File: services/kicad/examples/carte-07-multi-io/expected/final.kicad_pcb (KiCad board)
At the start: 2 copper layers, 99.5 x 79.8 mm, 44 parts, among them J1 IN_5V, J10 IO0, J11 IO1, J12 IO2, J2 SWD, U1 STM32F103C8T6, U2 AMS1117-3.3

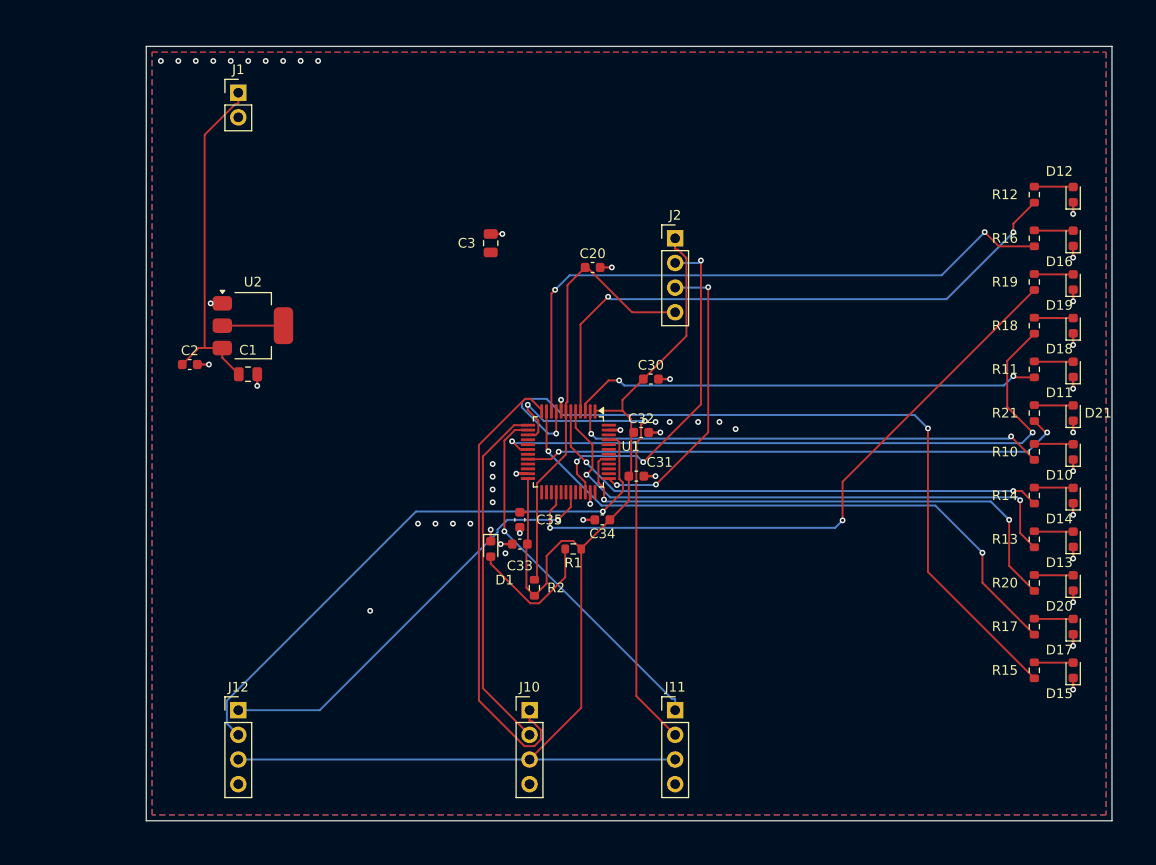
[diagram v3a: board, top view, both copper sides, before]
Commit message: chore(banc): relivrer carte-01..10 avec la couture corrigee
Boards reroutes par HTTP depuis placement.kicad_pcb inchange, avec le
code de #217. Juges par remesurer_banc.py : 0 erreur, 0 connexion
manquante sur les dix. 678 -> 443 vias ; la rangee de vias GND du bord
haut a disparu.

mesures.json : `board` recompte, `drc_du_board` rejuge, nouvelle cle
`couture_corrigee` (date, vias_avant, couches). journal.txt et les
champs du run d origine sont laisses tels quels et le disent.
rendu-3d.png : kicad-cli, modeles 3D, iso 1400x900.

Couches d un tirage : huit cartes sur 2, carte-08 et carte-10 sur 4.
CLAUDE.md et BANC_DRIVER_LLM.md recomptes. carte-11 non touchee.

Co-Authored-By: Claude Opus 5 (1M context) <noreply@anthropic.com>
Claude-Session: https://claude.ai/code/session_01TnMqm4La2CxQHHB5K8aSSV
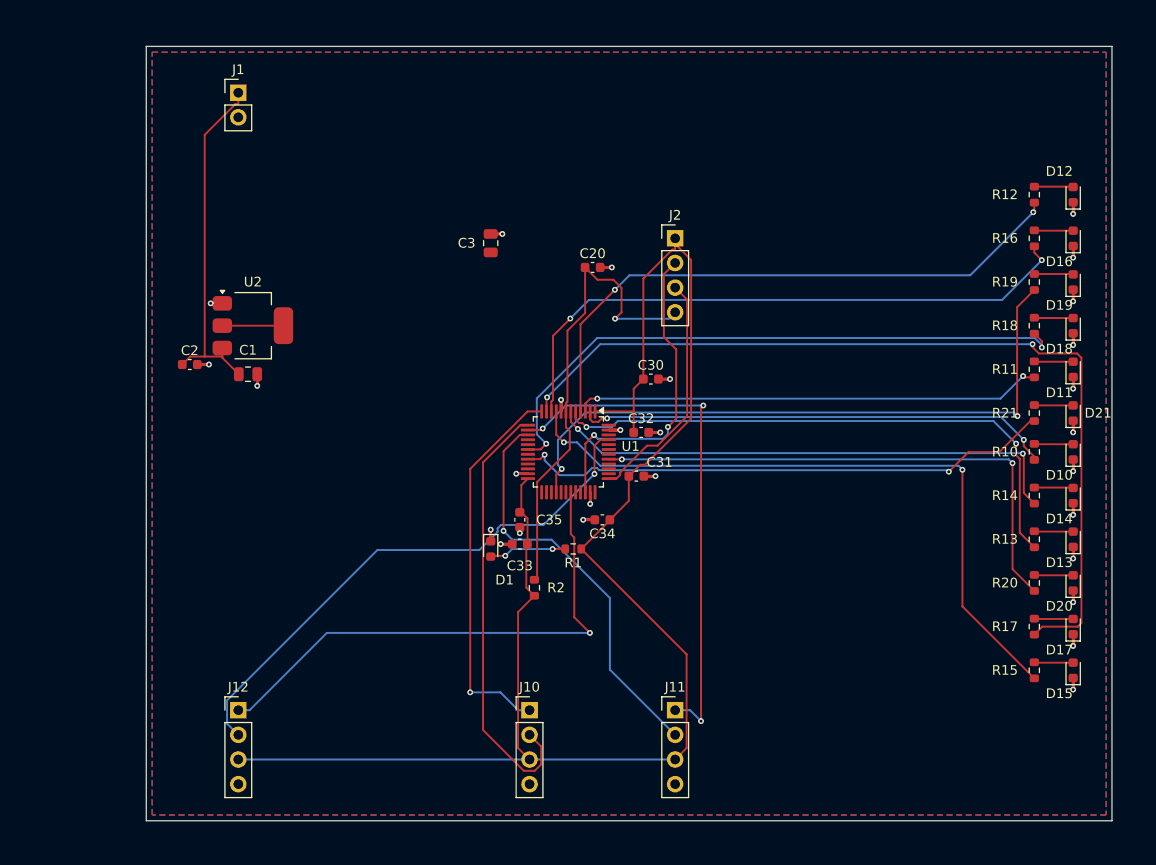
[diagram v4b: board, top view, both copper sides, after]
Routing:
- net GND: track 36.6 -> 103.8 mm, vias 53 -> 28
- net +3V3: track 132.4 -> 165.9 mm
- net IO_L7: track 63.9 -> 92.2 mm
- net EXT1_1: track 38.1 -> 54.8 mm, vias 1 -> 3
- net IO_L5: track 81.0 -> 70.3 mm
- net EXT2_1: track 44.6 -> 54.8 mm
- net EXT1_2: track 51.6 -> 42.1 mm, vias 2 -> 1
- net EXT0_2: track 36.6 -> 45.3 mm
- net EXT0_1: track 47.7 -> 39.7 mm, vias 0 -> 1
- net SWCLK: track 31.1 -> 24.6 mm, vias 3 -> 0
- net LED_PWR: track 14.1 -> 8.00 mm, vias 0 -> 2
- net IO_L8: track 68.6 -> 64.1 mm
- net EXT2_2: track 60.2 -> 56.4 mm
- net NRST: track 45.5 -> 49.2 mm, vias 0 -> 1
- net SWDIO: track 36.9 -> 33.2 mm, vias 3 -> 2
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
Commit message: fix(banc): le contour n etait JAMAIS resserre — dix cartes divisees par 2 a 4
Question de l utilisateur devant les rendus : « tu es satisfait de ce
placement ? ». Non, et la mesure lui donnait raison.

    carte-10 livree     140 x 105 mm = 14725 mm2
    son circuit          51 x  66 mm =  3366 mm2
    OCCUPATION                            23 %
    connecteurs                      56 a 75 mm du circuit
    fil de signal                      1230 mm  (VIN a lui seul 112 mm)

LA CAUSE : `run_pipeline.py` n envoyait pas `auto_size_board` a `/place/auto`.
Le resserrement du contour sur le placement existe depuis le 2026-09-13 et ne
s execute que si l appelant l autorise ; le defaut du modele est `False`.

C est le SEPTIEME levier de ce projet qui existe et que personne n appelle,
apres max_distance_mm, anchor_pin, WorkflowConfig.grid, constraints,
move_reference, bottom_up_placement et LocalRerouter.

⚠️ Et il etait INVISIBLE : la chaine de PRODUCTION passe bien le drapeau depuis
`handlePlacement`. Le banc mesurait donc un comportement que le produit n a
pas — l inverse exact de ce a quoi sert un banc.

MESURE APRES CORRECTION, meme circuit, meme graine :

    carte             demandee      REELLE        err  manq
    carte-01           25 x 20     20,1 x 14,6     0    0
    carte-02           55 x 40     34,9 x 25,4     0    0
    carte-03           50 x 35     26,1 x 20,1     0    0
    carte-04           60 x 45     36,6 x 27,2     0    0
    carte-05           70 x 50     43,6 x 32,6     0    0
    carte-06           80 x 60     48,5 x 36,4     0    0
    carte-07          110 x 80     53,2 x 38,8     0    0
    carte-08          125 x 95     56,4 x 44,1     0    0
    carte-09          130 x 100    57,3 x 45,2     0    0
    carte-10          140 x 105    61,0 x 45,8     0    0

Dix sur dix, 100 % route, aucune erreur, aucune connexion manquante. Sur
carte-10 : occupation 23 -> 56 %, fil de signal 1230 -> 652 mm, VIN 112 -> 45,5,
connecteurs 56-75 -> 23-35 mm.

ET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
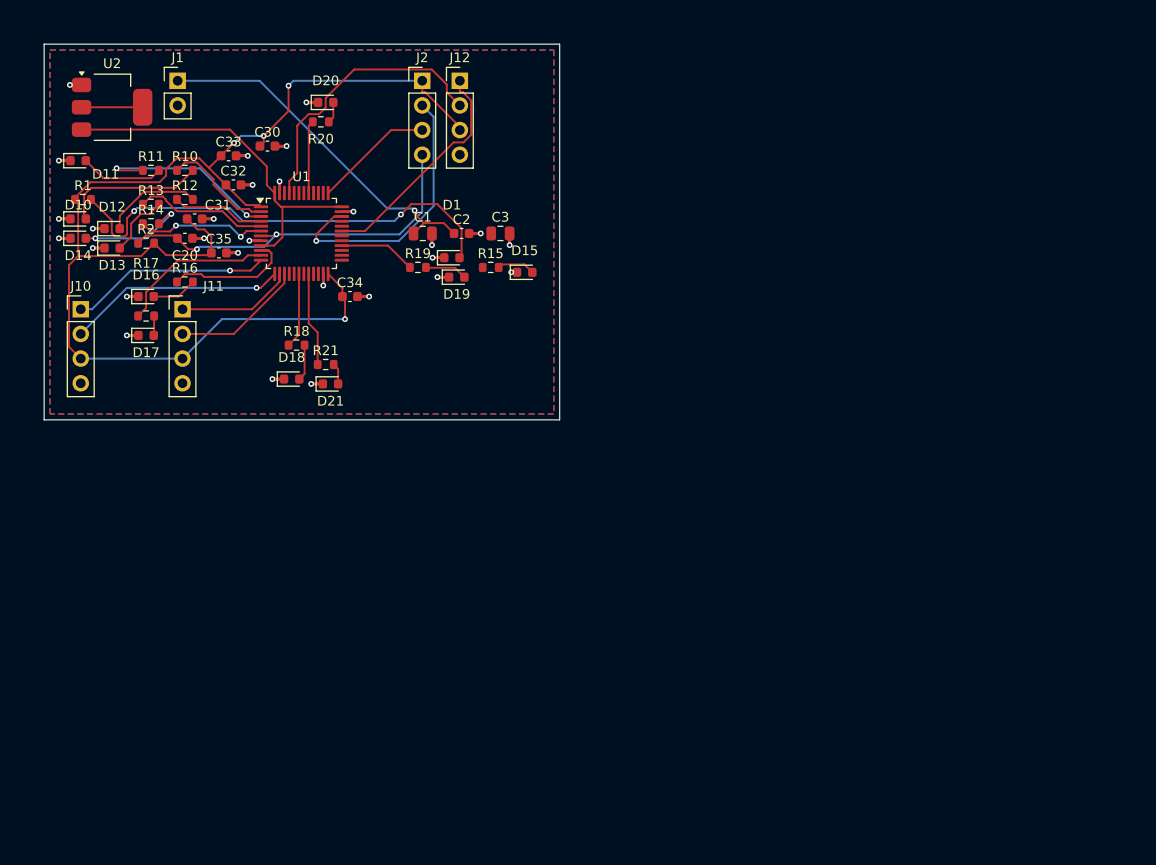
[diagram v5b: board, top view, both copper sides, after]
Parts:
- moved D14 105.9 mm to (97.0, 85.0), turned to 0 degrees
- moved D10 105.3 mm to (97.0, 83.0), turned to 0 degrees
- moved D11 104.7 mm to (97.0, 77.0), turned to 0 degrees
- moved D13 103.4 mm to (100.5, 86.0), turned to 0 degrees
- moved D17 100.1 mm to (104.0, 95.0), turned to 0 degrees
- moved D12 99.1 mm to (100.5, 84.0), turned to 0 degrees
- moved R13 97.3 mm to (104.5, 81.5), turned to 0 degrees
- moved R17 96.9 mm to (104.0, 93.0), turned to 0 degrees
- moved D16 95.7 mm to (104.0, 91.0), turned to 0 degrees
- moved R14 95.2 mm to (104.5, 83.5), turned to 0 degrees
- moved R11 93.3 mm to (104.5, 78.0), turned to 0 degrees
- moved R10 92.2 mm to (108.0, 78.0), turned to 0 degrees
- moved D20 91.5 mm to (122.5, 71.0), turned to 0 degrees
- moved R16 87.6 mm to (108.0, 89.5), turned to 0 degrees
- moved R20 87.5 mm to (122.0, 73.0), turned to 0 degrees
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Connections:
- U1 pad 36: Net-(U1-36) -> PWR_FLAG
- U1 pad 48: Net-(U1-48) -> PWR_FLAG
- U1 pad 9: IO_L5 -> PWR_FLAG
- U2 pad 3: VIN -> PWR_FLAG
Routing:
- net IO_L7: track 92.2 -> 16.2 mm, vias 2 -> 0
- net IO_L5: track 70.3 -> 0.00 mm, vias 2 -> 0
- net IO_L9: track 68.2 -> 7.94 mm, vias 2 -> 0
- net IO_L8: track 64.1 -> 7.78 mm, vias 2 -> 0
- net IO_L2: track 61.4 -> 9.59 mm, vias 2 -> 0
- net IO_L6: track 63.2 -> 13.0 mm, vias 2 -> 0
- net IO_L10: track 55.9 -> 7.51 mm, vias 2 -> 0
- net IO_L11: track 56.2 -> 9.72 mm, vias 2 -> 0
- net IO_L3: track 59.2 -> 13.8 mm, vias 2 -> 0
- net EXT1_1: track 54.8 -> 12.0 mm, vias 3 -> 0
- net IO_L4: track 54.6 -> 13.5 mm
- net LED_PWR: track 8.00 -> 48.1 mm
- net IO_L0: track 49.3 -> 11.5 mm, vias 2 -> 0
- net PWR_FLAG: track 0.00 -> 37.4 mm
- net +3V3: track 165.9 -> 130.3 mm, vias 0 -> 4
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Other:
- board size 99.5 x 79.8 mm -> 53.1 x 38.7 mm

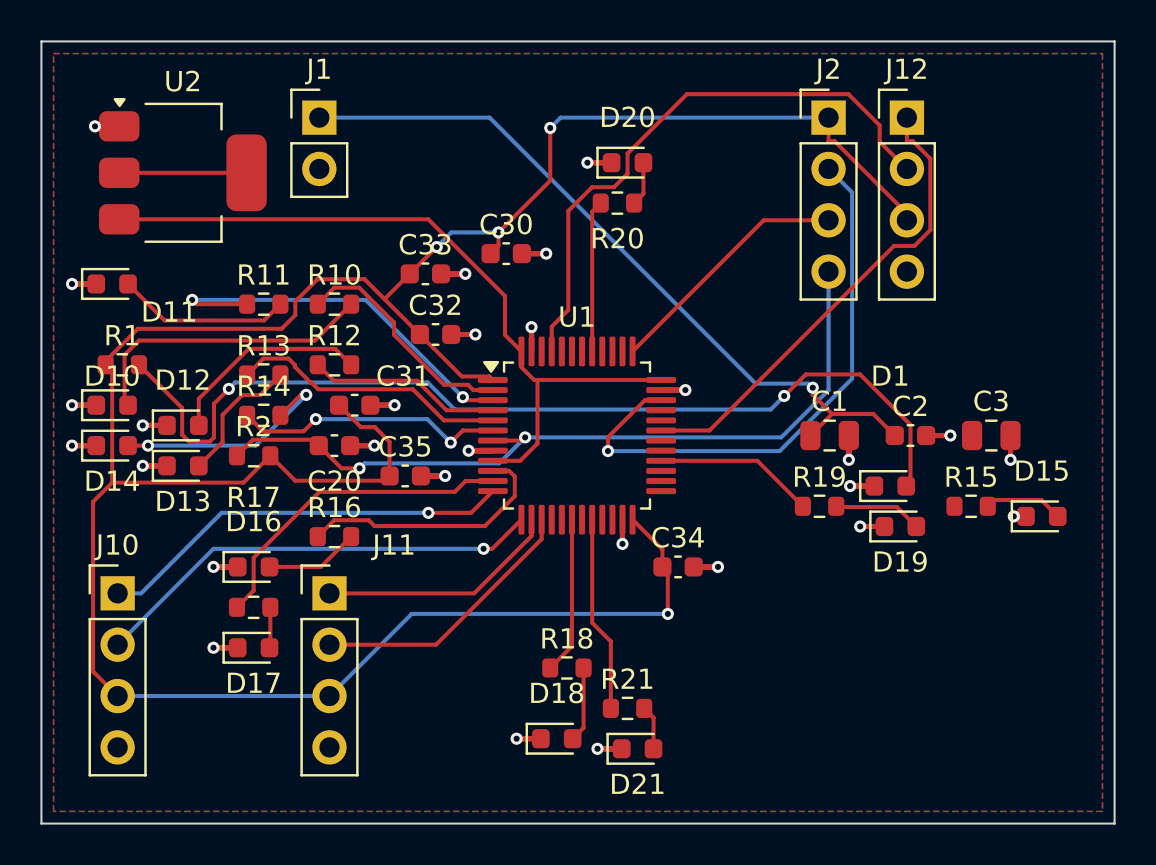
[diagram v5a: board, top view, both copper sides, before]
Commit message: feat(placement): les peripheriques se REPARTISSENT, ils ne s empilent plus
Question de l utilisateur devant le rendu : « c est quoi ce type de placement ? ».
Les composants s entassaient d un seul cote du boitier, etiquettes de
serigraphie l une sur l autre, trois quarts de la couronne vides.

TROIS CAUSES, toutes dans `_poser_les_peripheriques`, toutes la meme faute —
un angle unique pour tout un groupe :

  - les DIRECTS qui visent la meme broche (tous les decouplages d un rail,
    toutes les resistances d un meme signal) recevaient le MEME `angle_vers`
    et le meme rayon de depart ;
  - les SUIVEURS d un meme parent recevaient tous atan2(parent - centre) ;
  - les ISOLES partaient tous de l angle 0.0, c est-a-dire du meme point.

`le_long_du_rayon` ne s ecartait qu une fois la place prise : d ou la file.

REMEDE : `_ecart_en_eventail`. Le PREMIER de chaque groupe garde EXACTEMENT la
direction calculee — c est la topologie, on ne la perd pas pour faire joli — et
les suivants s ecartent symetriquement de 3 x `_PAS_ANGLE_DEG`.
Rien de deja pose ne bouge : seul l ANGLE DE DEPART de la recherche change, et
`le_long_du_rayon` reste seul juge de ce qui est libre.

BANC DES DIX CARTES, contour resserre ET peripheriques repartis :

    carte             demandee    livree         err  manq
    carte-01           25 x 20    20,1 x 13,6     0    0
    carte-02           55 x 40    34,9 x 25,2     0    0
    carte-03           50 x 35    27,6 x 19,9     0    0
    carte-04           60 x 45    36,6 x 29,8     0    0
    carte-05           70 x 50    40,0 x 32,6     0    0
    carte-06           80 x 60    46,5 x 36,4     0    0
    carte-07          110 x 80    47,7 x 38,8     0    0
    carte-08          125 x 95    57,4 x 44,1     0    0
    carte-09          130 x 100   57,8 x 45,2     0    0
    carte-10          140 x 105   59,0 x 45,8     0    0

Dix sur dix, 100 % route. carte-07 gagne 5,5 mm de largeur sur le passage
precedent, carte-06 deux, carte-10 deux. Sur ca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
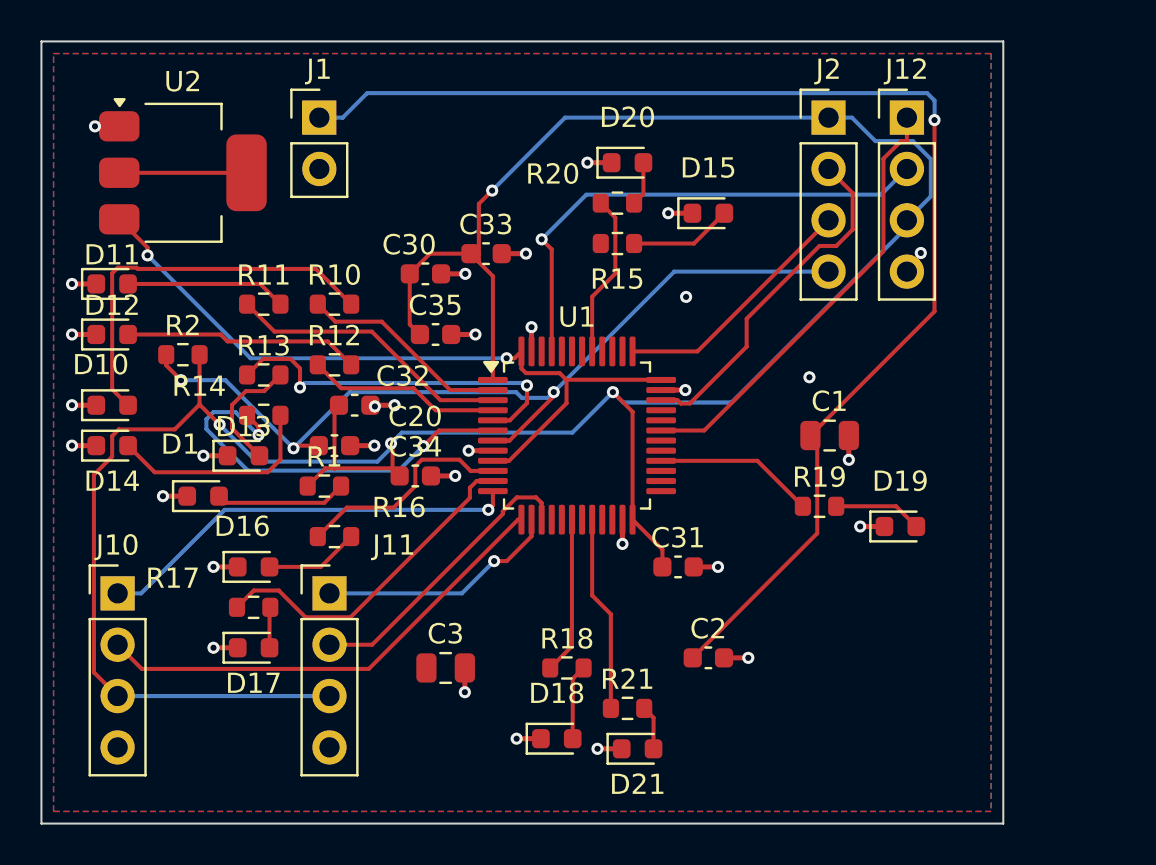
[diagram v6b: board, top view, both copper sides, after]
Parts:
- moved D1 34.0 mm to (101.5, 87.5)
- moved C3 29.3 mm to (113.5, 96.0)
- moved D15 22.3 mm to (126.5, 73.5)
- moved R15 21.8 mm to (122.0, 75.0)
- moved C31 17.9 mm to (125.0, 91.0)
- moved C2 14.9 mm to (126.5, 95.5)
- moved C34 13.8 mm to (112.0, 86.5)
- moved R1 11.7 mm to (107.5, 87.0)
- moved C35 7.16 mm to (113.0, 79.5)
- moved R2 6.10 mm to (100.5, 80.5)
- moved D12 5.70 mm to (97.0, 79.5)
- moved C32 5.32 mm to (109.0, 83.0)
- moved C30 4.12 mm to (112.5, 76.5)
- moved C33 3.16 mm to (115.5, 75.5)
- moved D13 3.04 mm to (103.5, 85.5)
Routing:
- net GND: track 103.8 -> 33.6 mm, vias 28 -> 32
- net LED_PWR: track 48.1 -> 6.52 mm, vias 2 -> 0
- net VIN: track 36.7 -> 63.9 mm
- net SWDIO: track 28.5 -> 17.4 mm, vias 1 -> 0
- net +3V3: track 130.3 -> 137.8 mm
- net IO_L4: track 13.5 -> 20.7 mm
- net IO_L1: track 19.7 -> 14.1 mm, vias 2 -> 0
- net NRST: track 39.3 -> 44.3 mm, vias 2 -> 3
- net LEDA0: track 14.8 -> 19.5 mm
- net IO_L3: track 13.8 -> 18.4 mm, vias 0 -> 2
- net EXT2_2: track 29.0 -> 25.3 mm, vias 0 -> 1
- net IO_L6: track 13.0 -> 11.0 mm
- net EXT2_1: track 23.6 -> 21.9 mm
- net LEDA2: track 10.2 -> 11.7 mm
- net LEDA5: track 3.93 -> 5.08 mm
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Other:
- board size 53.1 x 38.7 mm -> 47.6 x 38.7 mm

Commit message: docs(banc): les dix boards du banc du 2026-09-23, service corrige
Artefacts du banc dont le tableau est deja commite : les dix cartes a
100 % route, 0 erreur, 0 connexion manquante, chacune a la taille de son
circuit.

Co-Authored-By: Claude Opus 5 <noreply@anthropic.com>
Claude-Session: https://claude.ai/code/session_01TnMqm4La2CxQHHB5K8aSSV
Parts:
- moved R2 16.3 mm to (111.5, 92.5)
- moved D16 7.62 mm to (97.0, 94.0)
- moved C30 7.50 mm to (120.0, 76.5)
- moved C32 7.38 mm to (112.5, 76.5)
- moved R17 7.21 mm to (108.0, 87.0)
- moved D17 6.95 mm to (100.5, 89.0)
- moved D1 4.61 mm to (97.0, 88.5)
- moved J10 3.43 mm to (100.7, 92.3)
- moved R1 3.04 mm to (104.5, 87.5)
- moved R15 1.80 mm to (123.5, 76.0)
- moved D13 0.50 mm to (104.0, 85.5)
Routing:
- net VIN: track 63.9 -> 45.9 mm
- net LEDA6: track 4.66 -> 12.9 mm
- net IO_L4: track 20.7 -> 13.7 mm
- net LEDA7: track 2.02 -> 8.81 mm
- net PWR_FLAG: track 37.1 -> 43.2 mm, vias 2 -> 0
- net EXT0_2: track 23.5 -> 28.2 mm
- net IO_L3: track 18.4 -> 13.8 mm, vias 2 -> 0
- net IO_L6: track 11.0 -> 15.3 mm, vias 0 -> 2
- net EXT1_1: track 12.0 -> 16.1 mm
- net LEDA0: track 19.5 -> 15.5 mm, vias 0 -> 2
- net IO_L7: track 16.6 -> 12.7 mm, vias 0 -> 2
- net +3V3: track 137.8 -> 134.3 mm, vias 4 -> 1
- net EXT2_2: track 25.3 -> 22.6 mm
- net EXT1_2: track 14.5 -> 17.2 mm, vias 0 -> 1
- net LEDA4: track 10.5 -> 8.16 mm
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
